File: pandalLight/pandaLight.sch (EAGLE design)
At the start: 114 parts, among them J1 PJ-037A, U1 MIC2230-XXYML, U10 LEDS_CON, U11 LEDS_CON, U12 TPD12S016PWR, U13 M25P40-VMN, U14 PMOD-2X6, U15 PMOD-2X6, U16 PLR135-T10, U17 PLT133-T10W, U18 TP10SQ, U19 TP10SQ, U2 6SLX9TQG144, U20 PAN1322, U3 93LC46BT-I/OT, U4 FT2232HL, U5 TPD12S016PWR, U6 51, U7 51, U8 TXB0104RGYR, U9 100k, X1 USBUB-S, X2 HDMI_RECEPTICAL_A, X3 HDMI_RECEPTICAL_A, Y1 403, Y2 20Mhz

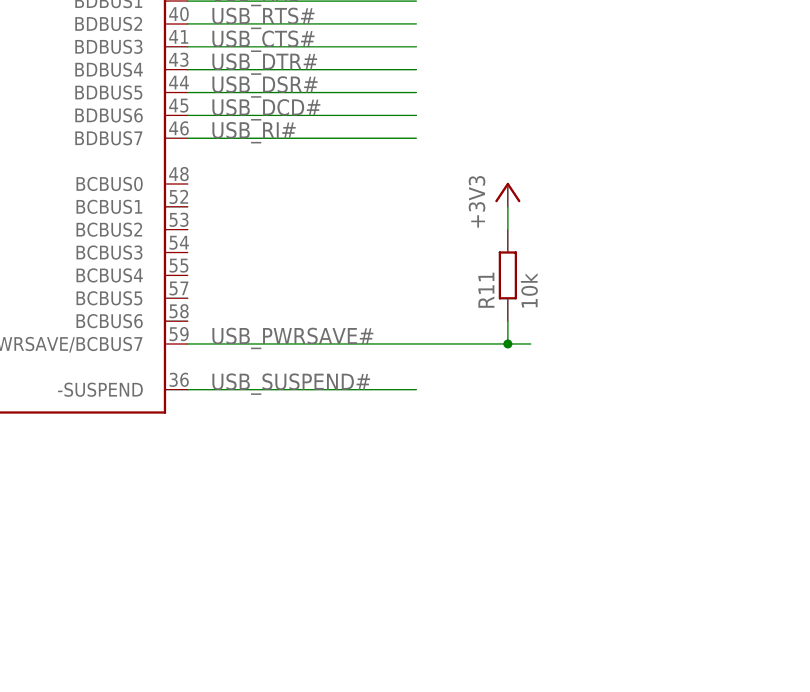
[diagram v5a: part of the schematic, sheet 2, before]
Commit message: Move S6LX9 to own library; Adjusted parts' "place" layer; USB_PWRSAV#
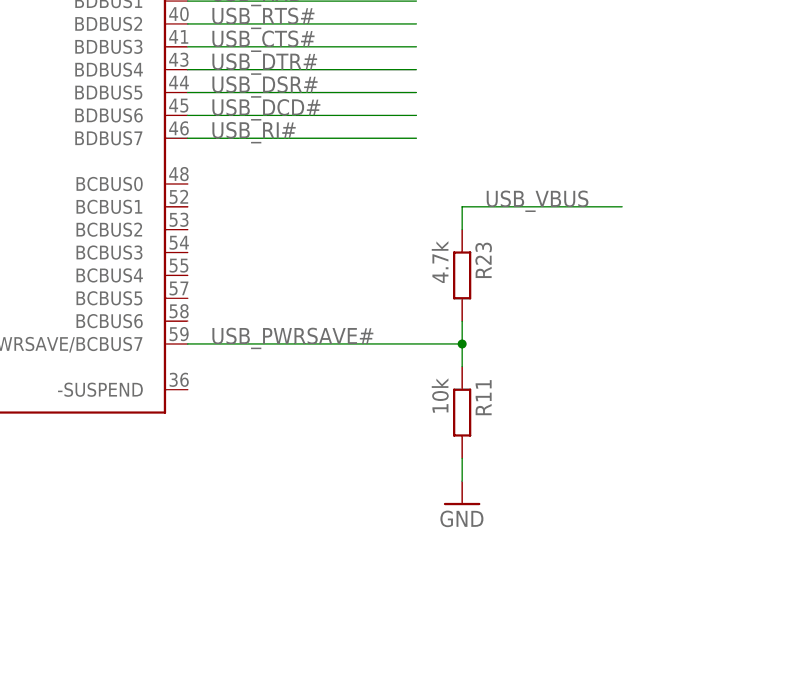
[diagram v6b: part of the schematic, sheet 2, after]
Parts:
- added R23: 4.7k, pandaLight:RESISTOR0402
- U2: device xilinx_devices_V6:6SLX9TQG144 -> pandaLight:6SLX9TQG144
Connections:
- removed net USB_SUSPEND#: U4.-SUSPEND
- net +3V3: no longer R11.2
- net GND: now also R11.2
- net USB_PWRSAVE#: now also R23.2
- net USB_VBUS: now also R23.1
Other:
- moved on the sheet: R11
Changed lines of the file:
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@@
 <attribute name="PARTNO" value="ERJ-2RKF1002X"/>
 </part>
-<part name="PS15" library="pandaLight" deviceset="+3V3" device=""/>
 <part name="C4" library="pandaLight" deviceset="CAPACITOR" device="1206" value="100u">
 <attribute name="PARTNO" value="CL31A107MQHNNNE"/>
@@
 <attribute name="PARTNO" value="741C083510JP"/>
 </part>
-<part name="U2" library="xilinx_devices_V6" deviceset="6SLX9TQG144" device="">
+<part name="U2" library="pandaLight" deviceset="6SLX9TQG144" device="">
 <attribute name="PARTNO" value="XC6SLX9-3TQG144C"/>
 </part>
@@
 <part name="GND31" library="pandaLight" deviceset="GND" device=""/>
 <part name="U$1" library="pandaLight" deviceset="ZENER_DIODE" device="" value="6V"/>
+<part name="R23" library="pandaLight" deviceset="RESISTOR" device="0402" value="4.7k">
+<attribute name="PARTNO" value="ERJ-2RKF1002X"/>
+</part>
+<part name="GND52" library="pandaLight" deviceset="GND" device=""/>
 </parts>
 <sheets>
@@
 <instance part="GND22" gate="1" x="243.84" y="106.68"/>
 <instance part="GND20" gate="1" x="210.82" y="144.78"/>
-<instance part="R11" gate="G$1" x="210.82" y="48.26" rot="R90">
-<attribute name="PARTNO" x="210.82" y="48.26" size="1.778" layer="96" display="off"/>
-</instance>
-<instance part="PS15" gate="G$1" x="210.82" y="58.42"/>
+<instance part="R11" gate="G$1" x="205.74" y="33.02" rot="R270">
+<attribute name="PARTNO" x="205.74" y="33.02" size="1.778" layer="96" rot="R180" display="off"/>
+</instance>
 <instance part="SV2" gate="1" x="185.42" y="106.68">
 <attribute name="PARTNO" x="185.42" y="106.68" size="1.778" layer="96" display="off"/>
@@
 <instance part="GND12" gate="1" x="27.94" y="27.94"/>
 <instance part="U2" gate="BNA" x="251.46" y="116.84" rot="R180"/>
+<instance part="R23" gate="G$1" x="205.74" y="48.26" rot="R270">
+<attribute name="PARTNO" x="205.74" y="48.26" size="1.778" layer="96" rot="R180" display="off"/>
+</instance>
+<instance part="GND52" gate="1" x="205.74" y="22.86"/>
 </instances>
 <busses>
@@
 <wire x1="27.94" y1="30.48" x2="27.94" y2="33.02" width="0.1524" layer="91"/>
 </segment>
+<segment>
+<pinref part="GND52" gate="1" pin="GND"/>
+<pinref part="R11" gate="G$1" pin="2"/>
+<wire x1="205.74" y1="25.4" x2="205.74" y2="27.94" width="0.1524" layer="91"/>
+</segment>
 </net>
 <net name="+3V3" class="1">
@@
 <wire x1="185.42" y1="162.56" x2="185.42" y2="160.02" width="0.1524" layer="91"/>
 <junction x="175.26" y="162.56"/>
-</segment>
-<segment>
-<pinref part="R11" gate="G$1" pin="2"/>
-<pinref part="PS15" gate="G$1" pin="+3V3"/>
-<wire x1="210.82" y1="53.34" x2="210.82" y2="55.88" width="0.1524" layer="91"/>
 </segment>
 <segment>
@@
 </segment>
 </net>
-<net name="USB_SUSPEND#" class="0">
-<segment>
-<pinref part="U4" gate="G$1" pin="-SUSPEND"/>
-<wire x1="175.26" y1="35.56" x2="200.66" y2="35.56" width="0.1524" layer="91"/>
-<label x="177.8" y="35.56" size="1.778" layer="95"/>
-</segment>
-</net>
 <net name="USB_TCK" class="0">
 <segment>
@@
 <segment>
 <pinref part="U4" gate="G$1" pin="PWRSAVE/BCBUS7"/>
-<wire x1="175.26" y1="40.64" x2="210.82" y2="40.64" width="0.1524" layer="91"/>
+<wire x1="175.26" y1="40.64" x2="205.74" y2="40.64" width="0.1524" layer="91"/>
 <label x="177.8" y="40.64" size="1.778" layer="95"/>
 <pinref part="R11" gate="G$1" pin="1"/>
-<wire x1="210.82" y1="40.64" x2="210.82" y2="43.18" width="0.1524" layer="91"/>
-<wire x1="210.82" y1="40.64" x2="213.36" y2="40.64" width="0.1524" layer="91"/>
-<junction x="210.82" y="40.64"/>
+<wire x1="205.74" y1="40.64" x2="205.74" y2="38.1" width="0.1524" layer="91"/>
+<pinref part="R23" gate="G$1" pin="2"/>
+<wire x1="205.74" y1="40.64" x2="205.74" y2="43.18" width="0.1524" layer="91"/>
+<junction x="205.74" y="40.64"/>
 </segment>
 </net>
@@
 <wire x1="10.16" y1="91.44" x2="38.1" y2="91.44" width="0.1524" layer="91"/>
 <label x="22.86" y="91.44" size="1.778" layer="95"/>
+</segment>
+<segment>
+<pinref part="R23" gate="G$1" pin="1"/>
+<wire x1="205.74" y1="53.34" x2="205.74" y2="55.88" width="0.1524" layer="91"/>
+<wire x1="205.74" y1="55.88" x2="223.52" y2="55.88" width="0.1524" layer="91"/>
+<label x="208.28" y="55.88" size="1.778" layer="95"/>
 </segment>
 </net>
@@
 <pinref part="U11" gate="G$1" pin="1"/>
 <wire x1="149.86" y1="5.08" x2="149.86" y2="27.94" width="0.1524" layer="91"/>
+<label x="137.16" y="27.94" size="1.778" layer="95"/>
+<wire x1="180.34" y1="27.94" x2="149.86" y2="27.94" width="0.1524" layer="91"/>
+<wire x1="149.86" y1="27.94" x2="134.62" y2="27.94" width="0.1524" layer="91"/>
 <junction x="149.86" y="27.94"/>
-<label x="137.16" y="27.94" size="1.778" layer="95"/>
-<wire x1="180.34" y1="27.94" x2="134.62" y2="27.94" width="0.1524" layer="91"/>
-</segment>
-</net>
+</segment>
+</net>

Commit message: Part renumber; "place" layer changes
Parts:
- removed C54: 0.1u, pandaLight:CAPACITOR0402
- removed U12: TPD12S016PWR, pandaLight:TPD12S016PWR
- removed U13: M25P40-VMN, pandaLight:M25P40-VMN
- removed U20: PAN1322, pandaLight:PAN1322
- added RN1, RN2: 51, pandaLight:741C083
- added RN3: 100k, pandaLight:741C083
- C10, C11, C41, C47: value 4.7u -> 0.47u; device pandaLight:CAPACITOR0603 -> pandaLight:CAPACITOR0402; PARTNO C0603C475K9PACTU -> C1005X5R0J474K050BB
- C12, C13: value 0.47u -> 10u; device pandaLight:CAPACITOR0402 -> pandaLight:CAPACITOR0603; PARTNO C1005X5R0J474K050BB -> CL10A106MQ8NNNC
- C14, C15: value 0.47u -> 4.7u; device pandaLight:CAPACITOR0402 -> pandaLight:CAPACITOR0603; PARTNO C1005X5R0J474K050BB -> C0603C475K9PACTU
- C17, C20, C22: value 4.7u -> 0.1u; device pandaLight:CAPACITOR0603 -> pandaLight:CAPACITOR0402; PARTNO C0603C475K9PACTU -> CL05B104KP5NNNC
- C18: value 27p -> 0.1u; PARTNO CL05C270JB5NNNC -> CL05B104KP5NNNC
- C19, C25, C46: value 0.1u -> 4.7u; device pandaLight:CAPACITOR0402 -> pandaLight:CAPACITOR0603; PARTNO CL05B104KP5NNNC -> C0603C475K9PACTU
- C23: value 27p -> 4.7u; device pandaLight:CAPACITOR0402 -> pandaLight:CAPACITOR0603; PARTNO CL05C270JB5NNNC -> C0603C475K9PACTU
- C28, C29: value 0.1u -> 27p; PARTNO CL05B104KP5NNNC -> CL05C270JB5NNNC
- C3, C4: value 100u -> 0.47u; device pandaLight:CAPACITOR1206 -> pandaLight:CAPACITOR0402; PARTNO CL31A107MQHNNNE -> C1005X5R0J474K050BB
- C43, C49: value 0.47u -> 0.1u; PARTNO C1005X5R0J474K050BB -> CL05B104KP5NNNC
- C5, C6: value 10u -> 100u; device pandaLight:CAPACITOR0603 -> pandaLight:CAPACITOR1206; PARTNO CL10A106MQ8NNNC -> CL31A107MQHNNNE
- JP2: value PMOD2-3_VCC_SEL -> PMOD0-1_VCC_SEL
- JP3: value PMOD0-1_VCC_SEL -> PMOD2-3_VCC_SEL
- R1: value 100k -> 1k; PARTNO ERJ-2RKF1003X -> ERJ-2RKF1001X
- R12: value 1k -> 2.2k; PARTNO ERJ-2RKF1001X -> ERJ-2RKF2201X
- R13: value 10k -> 1k; PARTNO ERJ-2RKF1002X -> ERJ-2RKF1001X
- R15: value 4.7k -> 10k; PARTNO ERJ-2RKF4701X -> ERJ-2RKF1002X
- R16: value 10k -> 2.4k; PARTNO ERJ-2RKF1002X -> ERJ-2RKF2401X
- R17: value 4.7k -> 100; PARTNO ERJ-2RKF4701X -> ERJ-2GEJ101X
- R18: value 100 -> 4.7k; PARTNO ERJ-2GEJ101X -> ERJ-2RKF4701X
- R20: value 2.4k -> 4.7k; PARTNO ERJ-2RKF2401X -> ERJ-2RKF4701X
- R21: value 4.7k -> 10k
- R4: value 1k -> 100k; PARTNO ERJ-2RKF1001X -> ERJ-2RKF1003X
- R6: value 10k -> 12k; PARTNO ERJ-2RKF1002X -> ERJ-2RKF1202X
- R8: value 2.2k -> 10k; PARTNO ERJ-2RKF2201X -> ERJ-2RKF1002X
- R9: value 12k -> 4.7k; PARTNO ERJ-2RKF1202X -> ERJ-2RKF1002X
- U1: value MIC2230-XXYML -> 6SLX9TQG144; device pandaLight:MIC2230-XXYML -> pandaLight:6SLX9TQG144; PARTNO MIC2230-S4YML TR -> XC6SLX9-3TQG144C
- U2: value 6SLX9TQG144 -> MIC2230-XXYML; device pandaLight:6SLX9TQG144 -> pandaLight:MIC2230-XXYML; PARTNO XC6SLX9-3TQG144C -> MIC2230-S4YML TR
- U3: value 93LC46BT-I/OT -> FT2232HL; device pandaLight:93LC46BT-I/OT -> pandaLight:FT2232HL; PARTNO 93LC46BT-I/OT -> FT2232HL-REEL
- U4: value FT2232HL -> 93LC46BT-I/OT; device pandaLight:FT2232HL -> pandaLight:93LC46BT-I/OT; PARTNO FT2232HL-REEL -> 93LC46BT-I/OT
- U6: value 51 -> TXB0104RGYR; device pandaLight:741C083 -> pandaLight:TXB0104RGYR; PARTNO 741C083510JP -> (none)
- U7: value 51 -> M25P40-VMN; device pandaLight:741C083 -> pandaLight:M25P40-VMN; PARTNO 741C083510JP -> M25P40-VMN6PB
- U8: value TXB0104RGYR -> TPD12S016PWR; device pandaLight:TXB0104RGYR -> pandaLight:TPD12S016PWR; PARTNO (none) -> TPD12S016PWR
- U9: value 100k -> PAN1322; device pandaLight:741C083 -> pandaLight:PAN1322; PARTNO (none) -> ENW-89841A3KF
- renumbered U$1 to D1, U10 to SV4, U11 to SV3, U14 to X5, U15 to X4, U16 to X6, U17 to X7, U18 to TP1, U19 to TP2
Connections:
- net +1V2: now also C1.1, C13.1, C2.1, C3.1, C4.1, L2.2, U1BVCCINT.VCCINT@0, U1BVCCINT.VCCINT@1, U1BVCCINT.VCCINT@2, U1BVCCINT.VCCINT@3, U1BVCCINT.VCCINT@4, U2.OUT2; no longer C10.1, C12.1, C14.1, C6.1, C8.1, L1.2, U1.OUT2, U2BVCCINT.VCCINT@0, U2BVCCINT.VCCINT@1, U2BVCCINT.VCCINT@2, U2BVCCINT.VCCINT@3, U2BVCCINT.VCCINT@4
- net +1V8: now also C19.1, C20.1, C21.1, C22.1, U3.VCORE@1, U3.VCORE@2, U3.VCORE@3, U3.VREGOUT; no longer C27.1, C28.1, C29.1, C30.1, U4.VCORE@1, U4.VCORE@2, U4.VCORE@3, U4.VREGOUT
- net +3V3: now also C10.1, C12.1, C17.1, C18.1, C27.1, C30.1, C40.1, C46.1, C51.1, C8.1, L1.2, R10.2, R13.2, R16.2, R18.2, R3.1, R5.1, R8.2, RN1.5, RN1.6, RN1.7, RN1.8, RN2.5, RN2.6, RN2.7, RN2.8, U1B0.VCCO_0@0, U1B0.VCCO_0@1, U1B0.VCCO_0@2, U1B1.VCCO_1@0, U1B1.VCCO_1@1, U1B1.VCCO_1@2, U1B2.IO_L1N_M0_CMPMISO_2, U1B2.VCCO_2@0, U1B2.VCCO_2@1, U1B3.VCCO_3@0, U1B3.VCCO_3@1, U1B3.VCCO_3@2, U1BVCCAUX.VCCAUX@0, U1BVCCAUX.VCCAUX@1, U1BVCCAUX.VCCAUX@2, U1BVCCAUX.VCCAUX@3, U1BVCCAUX.VCCAUX@4, U2.OUT1, U3.VCCIO@1, U3.VCCIO@2, U3.VCCIO@3, U3.VCCIO@4, U3.VREGIN, U4.VCC, U6.OE, U6.VCCA, U7.HOLD#, U7.VCC, U7.W#, U9.ONOFF, U9.VDD1, U9.VDDUART, U9.VSUPPLY@A4, U9.VSUPPLY@A5, U9.VSUPPLY@A6; no longer C13.1, C15.1, C22.1, C24.1, C25.1, C26.1, C43.1, C5.1, C50.1, C54.1, L2.2, R1.1, R10.1, R12.2, R15.2, R19.2, R5.2, R6.2, U1.OUT1, U12.VCCA, U13.HOLD#, U13.VCC, U13.W#, U20.ONOFF, U20.VDD1, U20.VDDUART, U20.VSUPPLY@A4, U20.VSUPPLY@A5, U20.VSUPPLY@A6, U2B0.VCCO_0@0, U2B0.VCCO_0@1, U2B0.VCCO_0@2, U2B1.VCCO_1@0, U2B1.VCCO_1@1, U2B1.VCCO_1@2, U2B2.IO_L1N_M0_CMPMISO_2, U2B2.VCCO_2@0, U2B2.VCCO_2@1, U2B3.VCCO_3@0, U2B3.VCCO_3@1, U2B3.VCCO_3@2, U2BVCCAUX.VCCAUX@0, U2BVCCAUX.VCCAUX@1, U2BVCCAUX.VCCAUX@2, U2BVCCAUX.VCCAUX@3, U2BVCCAUX.VCCAUX@4, U3.VCC, U4.VCCIO@1, U4.VCCIO@2, U4.VCCIO@3, U4.VCCIO@4, U4.VREGIN, U6.5, U6.6, U6.7, U6.8, U7.5, U7.6, U7.7, U7.8, U8.OE
- net +5V: now also C14.1, C15.1, C5.1, R1.2, R4.1, U2.AVIN, U2.VIN, U6.VCCB, U8.VCC5V; no longer C1.1, C2.1, C4.1, C40.1, R3.1, R4.2, U1.AVIN, U1.VIN, U12.VCC5V, U8.VCCB
- net 5V_SUP: now also C6.1; no longer C3.1
- net BT_CTS: now also U1B3.IO_L2N_3, U9.P0.7_UARTCTS; no longer U20.P0.7_UARTCTS, U2B3.IO_L2N_3
- net BT_RESET#: now also R23.2, U1B3.IO_L49N_3, U9.RESET#; no longer R21.2, U20.RESET#, U2B3.IO_L49N_3
- net BT_RTS: now also U1B3.IO_L1N_VREF_3, U9.P0.6_UARTRTS; no longer U20.P0.6_UARTRTS, U2B3.IO_L1N_VREF_3
- net BT_RX: now also U1B3.IO_L36P_3, U9.P0.5_UARTRXD; no longer U20.P0.5_UARTRXD, U2B3.IO_L36P_3
- net BT_TX: now also U1B3.IO_L2P_3, U9.P0.4_UARTTXD; no longer U20.P0.4_UARTTXD, U2B3.IO_L2P_3
- net BT_WAKE: now also U1B3.IO_L36N_3, U9.P0.14_LPMIN; no longer U20.P0.14_LPMIN, U2B3.IO_L36N_3
- net FPGA_CLK20: now also U1B3.IO_L83P_3; no longer U2B3.IO_L83P_3
- net GND: now also R15.1, R19.1, R23.1, R6.1, RN3.1, RN3.2, RN3.3, RN3.4, U1B2.IO_L13P_M1_2, U1BGND.GND@0, U1BGND.GND@1, U1BGND.GND@10, U1BGND.GND@11, U1BGND.GND@12, U1BGND.GND@2, U1BGND.GND@3, U1BGND.GND@4, U1BGND.GND@5, U1BGND.GND@6, U1BGND.GND@7, U1BGND.GND@8, U1BGND.GND@9, U1BNA.SUSPEND, U2.AGND, U2.EP, U2.PGND, U3.AGND, U3.GND@1, U3.GND@2, U3.GND@3, U3.GND@4, U3.GND@5, U3.GND@6, U3.GND@7, U3.GND@8, U3.TEST, U4.VSS, U6.EP, U6.GND, U7.VSS, U8.GND@0, U8.GND@1, U8.GND@2, U9.VSS@A1, U9.VSS@A11, U9.VSS@A12, U9.VSS@A7, U9.VSS@A9, U9.VSS@C8, U9.VSS@C9, U9.VSS@D7, U9.VSS@D8, U9.VSS@E8, U9.VSS@E9, U9.VSS@F1, U9.VSS@F11, U9.VSS@F12, U9.VSS@F9; no longer C54.2, R13.1, R16.1, R18.1, R9.1, U1.AGND, U1.EP, U1.PGND, U12.GND@0, U12.GND@1, U12.GND@2, U13.VSS, U20.VSS@A1, U20.VSS@A11, U20.VSS@A12, U20.VSS@A7, U20.VSS@A9, U20.VSS@C8, U20.VSS@C9, U20.VSS@D7, U20.VSS@D8, U20.VSS@E8, U20.VSS@E9, U20.VSS@F1, U20.VSS@F11, U20.VSS@F12, U20.VSS@F9, U2B2.IO_L13P_M1_2, U2BGND.GND@0, U2BGND.GND@1, U2BGND.GND@10, U2BGND.GND@11, U2BGND.GND@12, U2BGND.GND@2, U2BGND.GND@3, U2BGND.GND@4, U2BGND.GND@5, U2BGND.GND@6, U2BGND.GND@7, U2BGND.GND@8, U2BGND.GND@9, U2BNA.SUSPEND, U3.VSS, U4.AGND, U4.GND@1, U4.GND@2, U4.GND@3, U4.GND@4, U4.GND@5, U4.GND@6, U4.GND@7, U4.GND@8, U4.TEST, U8.EP, U8.GND, U9.1, U9.2, U9.3, U9.4
- net HDMI_RX_CEC_3V3: now also U1B0.IO_L35P_GCLK17_0; no longer U2B0.IO_L35P_GCLK17_0
- net HDMI_RX_CLK_N: now also RN2.4, U1B0.IO_L34N_GCLK18_0; no longer U2B0.IO_L34N_GCLK18_0, U7.4
- net HDMI_RX_CLK_P: now also RN2.3, U1B0.IO_L34P_GCLK19_0; no longer U2B0.IO_L34P_GCLK19_0, U7.3
- net HDMI_RX_CTRL_EN: now also R15.2, U1B0.IO_L36N_GCLK14_0; no longer R13.2, U2B0.IO_L36N_GCLK14_0
- net HDMI_RX_DATA0_N: now also RN2.2, U1B0.IO_L4N_0; no longer U2B0.IO_L4N_0, U7.2
- net HDMI_RX_DATA0_P: now also RN2.1, U1B0.IO_L4P_0; no longer U2B0.IO_L4P_0, U7.1
- net HDMI_RX_DATA1_N: now also RN1.4, U1B0.IO_L3N_0; no longer U2B0.IO_L3N_0, U6.4
- net HDMI_RX_DATA1_P: now also RN1.3, U1B0.IO_L3P_0; no longer U2B0.IO_L3P_0, U6.3
- net HDMI_RX_DATA2_N: now also RN1.2, U1B0.IO_L2N_0; no longer U2B0.IO_L2N_0, U6.2
- net HDMI_RX_DATA2_P: now also RN1.1, U1B0.IO_L2P_0; no longer U2B0.IO_L2P_0, U6.1
- net HDMI_RX_SCL_3V3: now also U1B0.IO_L35N_GCLK16_0; no longer U2B0.IO_L35N_GCLK16_0
- net HDMI_RX_SDA_3V3: now also U1B0.IO_L36P_GCLK15_0; no longer U2B0.IO_L36P_GCLK15_0
- net HDMI_TX_5V: now also C43.1, U8.5V_OUT; no longer C46.1, U12.5V_OUT
- net HDMI_TX_CEC: now also U8.CEC_B; no longer U12.CEC_B
- net HDMI_TX_CEC_3V3: now also U1B2.IO_L48P_D7_2, U8.CEC_A; no longer U12.CEC_A, U2B2.IO_L48P_D7_2
- net HDMI_TX_CLK_N: now also U1B2.IO_L31N_GCLK30_D15_2, U8.CLK-; no longer U12.CLK-, U2B2.IO_L31N_GCLK30_D15_2
- net HDMI_TX_CLK_P: now also U1B2.IO_L31P_GCLK31_D14_2, U8.CLK+; no longer U12.CLK+, U2B2.IO_L31P_GCLK31_D14_2
- net HDMI_TX_CTRL_EN: now also R21.2, U1B2.IO_L49N_D4_2, U8.CT_HPD, U8.LS_OE; no longer R16.2, U12.CT_HPD, U12.LS_OE, U2B2.IO_L49N_D4_2
- net HDMI_TX_DATA0_N: now also U1B2.IO_L30N_GCLK0_USERCCLK_2, U8.D0-; no longer U12.D0-, U2B2.IO_L30N_GCLK0_USERCCLK_2
- net HDMI_TX_DATA0_P: now also U1B2.IO_L30P_GCLK1_D13_2, U8.D0+; no longer U12.D0+, U2B2.IO_L30P_GCLK1_D13_2
- net HDMI_TX_DATA1_N: now also U1B2.IO_L14N_D12_2, U8.D1-; no longer U12.D1-, U2B2.IO_L14N_D12_2
- net HDMI_TX_DATA1_P: now also U1B2.IO_L14P_D11_2, U8.D1+; no longer U12.D1+, U2B2.IO_L14P_D11_2
- net HDMI_TX_DATA2_N: now also U1B2.IO_L12N_D2_MISO3_2, U8.D2-; no longer U12.D2-, U2B2.IO_L12N_D2_MISO3_2
- net HDMI_TX_DATA2_P: now also U1B2.IO_L12P_D1_MISO2_2, U8.D2+; no longer U12.D2+, U2B2.IO_L12P_D1_MISO2_2
- net HDMI_TX_HPD_5V: now also U8.HPD_B; no longer U12.HPD_B
- net HDMI_TX_SCL_3V3: now also U1B2.IO_L48N_RDWR_B_VREF_2, U8.SCL_A; no longer U12.SCL_A, U2B2.IO_L48N_RDWR_B_VREF_2
- net HDMI_TX_SCL_5V: now also U8.SCL_B; no longer U12.SCL_B
- net HDMI_TX_SDA_3V3: now also U1B2.IO_L49P_D3_2, U8.SDA_A; no longer U12.SDA_A, U2B2.IO_L49P_D3_2
- net HDMI_TX_SDA_5V: now also U8.SDA_B; no longer U12.SDA_B
- net LEDS0_CLK: now also U1B1.IO_L47N_1, U6.A4; no longer U2B1.IO_L47N_1, U8.A4
- net LEDS0_CLK_5V: now also RN3.8, U6.B4; no longer U8.B4, U9.8
- net LEDS0_DATA: now also U1B1.IO_L46P_1, U6.A1; no longer U2B1.IO_L46P_1, U8.A1
- net LEDS0_DATA_5V: now also RN3.5, U6.B1; no longer U8.B1, U9.5
- net LEDS1_CLK: now also U1B1.IO_L46N_1, U6.A2; no longer U2B1.IO_L46N_1, U8.A2
- net LEDS1_CLK_5V: now also RN3.6, U6.B2; no longer U8.B2, U9.6
- net LEDS1_DATA: now also U1B1.IO_L47P_1, U6.A3; no longer U2B1.IO_L47P_1, U8.A3
- net LEDS1_DATA_5V: now also RN3.7, U6.B3; no longer U8.B3, U9.7
- net N$1: now also C29.1, U3.XTIN; no longer C23.1, U4.XTIN
- net N$10: now also R12.2, U3.EEDATA, U4.DI; no longer R8.2, U3.DI, U4.EEDATA
- net N$11: now also R6.2, U3.REF; no longer R9.2, U4.REF
- net N$12: now also R10.1, R12.1, U4.DO; no longer R7.1, R8.1, U3.DO
- net N$13: now also R5.2, U3.-RESET; no longer R10.2, U4.-RESET
- net N$19: now also U9.P0.12_SDA0; no longer U20.P0.12_SDA0
- net N$25: now also R2.2, U2.EN1; no longer R3.2, U1.EN1
- net N$27: now also R3.2, U2.EN2; no longer R1.2, U1.EN2
- net N$28: now also C25.1, C26.1, FB2.2, U3.VPHY; no longer C20.1, C21.1, FB1.2, U4.VPHY
- net N$29: now also U9.P0.13_SCL0; no longer U20.P0.13_SCL0
- net N$31: now also C23.1, C24.1, FB1.2, U3.VPLL; no longer C17.1, C19.1, FB2.2, U4.VPLL
- net N$34: now also R18.1, U1B2.PROGRAM_B_2; no longer R17.1, U2B2.PROGRAM_B_2
- net N$35: now also R13.1, U1B0.IO_L1P_HSWAPEN_0; no longer R12.1, U2B0.IO_L1P_HSWAPEN_0
- net N$36: now also C50.1; no longer C51.1
- net N$39: now also R20.1, U1B2.IO_L65P_INIT_B_2; no longer R15.1, U2B2.IO_L65P_INIT_B_2
- net N$4: now also R4.2, U2.FPWM#; no longer R2.2, U1.FPWM#
- net N$40: now also U1B2.IO_L3N_MOSI_CSI_B_MISO0_2, U7.DQ0; no longer U13.DQ0, U2B2.IO_L3N_MOSI_CSI_B_MISO0_2
- net N$41: now also R16.1, U1B2.IO_L65N_CSO_B_2, U7.S#; no longer R20.1, U13.S#, U2B2.IO_L65N_CSO_B_2
- net N$42: now also R17.1, R19.2, U1B2.IO_L1P_CCLK_2, U7.C; no longer R18.2, R19.1, U13.C, U2B2.IO_L1P_CCLK_2
- net N$43: now also U1B2.IO_L3P_D0_DIN_MISO_MISO1_2, U7.DQ1; no longer U13.DQ1, U2B2.IO_L3P_D0_DIN_MISO_MISO1_2
- net N$47: now also R1.1; no longer R4.1
- net N$49: now also JP3.2; no longer JP2.2
- net N$5: now also C28.1, U3.XTOUT; no longer C18.1, U4.XTOUT
- net N$51: now also JP2.2; no longer JP3.2
- net N$6: now also R7.1, U3.EECS, U4.CS; no longer R5.1, U3.CS, U4.EECS
- net N$7: now also U3.D-; no longer U4.D-
- net N$8: now also U3.D+; no longer U4.D+
- net N$9: now also R8.1, U3.EESK, U4.CLK; no longer R6.1, U3.CLK, U4.EESK
- net PMOD0_0: now also U1B1.IO_L32P_1; no longer U2B1.IO_L32P_1
- net PMOD0_1: now also U1B1.IO_L33P_1; no longer U2B1.IO_L33P_1
- net PMOD0_2: now also U1B1.IO_L34P_1; no longer U2B1.IO_L34P_1
- net PMOD0_3: now also U1B1.IO_L40P_GCLK11_1; no longer U2B1.IO_L40P_GCLK11_1
- net PMOD1_0: now also U1B1.IO_L1N_VREF_1; no longer U2B1.IO_L1N_VREF_1
- net PMOD1_1: now also U1B1.IO_L32N_1; no longer U2B1.IO_L32N_1
- net PMOD1_2: now also U1B1.IO_L33N_1; no longer U2B1.IO_L33N_1
- net PMOD1_3: now also U1B1.IO_L34N_1; no longer U2B1.IO_L34N_1
- net PMOD2_0: now also U1B0.IO_L62P_0; no longer U2B0.IO_L62P_0
- net PMOD2_1: now also U1B0.IO_L63P_SCP7_0; no longer U2B0.IO_L63P_SCP7_0
- net PMOD2_2: now also U1B0.IO_L64P_SCP5_0; no longer U2B0.IO_L64P_SCP5_0
- net PMOD2_3: now also U1B0.IO_L65P_SCP3_0; no longer U2B0.IO_L65P_SCP3_0
- net PMOD3_0: now also U1B0.IO_L37N_GCLK12_0; no longer U2B0.IO_L37N_GCLK12_0
- net PMOD3_1: now also U1B0.IO_L62N_VREF_0; no longer U2B0.IO_L62N_VREF_0
- net PMOD3_2: now also U1B0.IO_L63N_SCP6_0; no longer U2B0.IO_L63N_SCP6_0
- net PMOD3_3: now also U1B0.IO_L64N_SCP4_0; no longer U2B0.IO_L64N_SCP4_0
- net SW1: now also L1.1, U2.SW1; no longer L2.1, U1.SW1
- net SW2: now also L2.1, U2.SW2; no longer L1.1, U1.SW2
- net TOS_IN: now also U1B3.IO_L83N_VREF_3; no longer U2B3.IO_L83N_VREF_3
- net TOS_OUT: now also U1B3.IO_L1P_3; no longer U2B3.IO_L1P_3
- net USB_CTS#: now also U1B1.IO_L42P_GCLK7_1, U3.BDBUS3; no longer U2B1.IO_L42P_GCLK7_1, U4.BDBUS3
- net USB_DCD#: now also U1B1.IO_L43N_GCLK4_1, U3.BDBUS6; no longer U2B1.IO_L43N_GCLK4_1, U4.BDBUS6
- net USB_DSR#: now also U1B1.IO_L43P_GCLK5_1, U3.BDBUS5; no longer U2B1.IO_L43P_GCLK5_1, U4.BDBUS5
- net USB_DTR#: now also U1B1.IO_L42N_GCLK6_TRDY1_1, U3.BDBUS4; no longer U2B1.IO_L42N_GCLK6_TRDY1_1, U4.BDBUS4
- net USB_PWRSAVE#: now also R9.2, U3.PWRSAVE/BCBUS7; no longer R23.2, U4.PWRSAVE/BCBUS7
- net USB_RI#: now also U1B1.IO_L45P_1, U3.BDBUS7; no longer U2B1.IO_L45P_1, U4.BDBUS7
- net USB_RTS#: now also U1B1.IO_L41N_GCLK8_1, U3.BDBUS2; no longer U2B1.IO_L41N_GCLK8_1, U4.BDBUS2
- net USB_RXD: now also U1B1.IO_L41P_GCLK9_IRDY1_1, U3.BDBUS1; no longer U2B1.IO_L41P_GCLK9_IRDY1_1, U4.BDBUS1
- net USB_TCK: now also U1BNA.TCK, U3.ADBUS0; no longer U2BNA.TCK, U4.ADBUS0
- net USB_TDI: now also U1BNA.TDI, U3.ADBUS1; no longer U2BNA.TDI, U4.ADBUS1
- net USB_TDO: now also U1BNA.TDO, U3.ADBUS2; no longer U2BNA.TDO, U4.ADBUS2
- net USB_TMS: now also U1BNA.TMS, U3.ADBUS3; no longer U2BNA.TMS, U4.ADBUS3
- net USB_TXD: now also U1B1.IO_L40N_GCLK10_1, U3.BDBUS0; no longer U2B1.IO_L40N_GCLK10_1, U4.BDBUS0
- net USB_VBUS: now also R9.1; no longer R23.1

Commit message: Changed all 7mil traces to 6mil; Set library part prefixes; Applied all part attributes
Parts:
- D1: PARTNO (none) -> SMAJ6.0A
- R23, R9: PARTNO ERJ-2RKF1002X -> ERJ-2RKF4701X
- RN3: PARTNO (none) -> 741C083104JP
- U6: PARTNO (none) -> TXB0104RGYR
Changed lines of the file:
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@@
 <part name="GND49" library="pandaLight" deviceset="GND" device=""/>
 <part name="R23" library="pandaLight" deviceset="RESISTOR" device="0402" value="4.7k">
-<attribute name="PARTNO" value="ERJ-2RKF1002X"/>
+<attribute name="PARTNO" value="ERJ-2RKF4701X"/>
 </part>
 <part name="GND50" library="pandaLight" deviceset="GND" device=""/>
@@
 <part name="PS21" library="pandaLight" deviceset="+3V3" device=""/>
 <part name="GND29" library="pandaLight" deviceset="GND" device=""/>
-<part name="U6" library="pandaLight" deviceset="TXB0104" device="RGYR"/>
-<part name="RN3" library="pandaLight" deviceset="741C083" device="" value="100k"/>
+<part name="U6" library="pandaLight" deviceset="TXB0104" device="RGYR">
+<attribute name="PARTNO" value="TXB0104RGYR"/>
+</part>
+<part name="RN3" library="pandaLight" deviceset="741C083" device="" value="100k">
+<attribute name="PARTNO" value="741C083104JP"/>
+</part>
 <part name="SV4" library="pandaLight" deviceset="MA04-1" device="" value="LEDS_CON">
 <attribute name="BOM" value="EXCLUDE"/>
@@
 <attribute name="PARTNO" value="C1005X5R0J474K050BB"/>
 </part>
-<part name="D1" library="pandaLight" deviceset="ZENER_DIODE" device="" value="6V"/>
+<part name="D1" library="pandaLight" deviceset="ZENER_DIODE" device="" value="6V">
+<attribute name="PARTNO" value="SMAJ6.0A"/>
+</part>
 <part name="R9" library="pandaLight" deviceset="RESISTOR" device="0402" value="4.7k">
-<attribute name="PARTNO" value="ERJ-2RKF1002X"/>
+<attribute name="PARTNO" value="ERJ-2RKF4701X"/>
 </part>
 <part name="GND22" library="pandaLight" deviceset="GND" device=""/>
@@
 <attribute name="PARTNO" x="185.42" y="81.28" size="1.778" layer="96" display="off"/>
 </instance>
-<instance part="D1" gate="G$1" x="40.64" y="106.68" rot="R90"/>
+<instance part="D1" gate="G$1" x="40.64" y="106.68" rot="R90">
+<attribute name="PARTNO" x="40.64" y="106.68" size="1.778" layer="96" display="off"/>
+</instance>
 </instances>
 <busses>
@@
 <instance part="PS21" gate="G$1" x="63.5" y="35.56"/>
 <instance part="GND29" gate="1" x="63.5" y="-5.08"/>
-<instance part="U6" gate="G$1" x="81.28" y="15.24"/>
-<instance part="RN3" gate="G$1" x="121.92" y="7.62" rot="R90"/>
+<instance part="U6" gate="G$1" x="81.28" y="15.24">
+<attribute name="PARTNO" x="81.28" y="15.24" size="1.778" layer="96" display="off"/>
+</instance>
+<instance part="RN3" gate="G$1" x="121.92" y="7.62" rot="R90">
+<attribute name="PARTNO" x="121.92" y="7.62" size="1.778" layer="96" display="off"/>
+</instance>
 <instance part="SV4" gate="G$1" x="187.96" y="0" rot="R180">
 <attribute name="PARTNO" x="187.96" y="0" size="1.778" layer="96" display="off"/>
